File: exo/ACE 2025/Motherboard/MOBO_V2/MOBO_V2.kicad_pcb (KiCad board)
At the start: 4 copper layers, 100 x 100 mm, 70 parts, among them J301 USB_C_UART, J302 USB_C_DEBUG, J601 Conn_02x10_Counter_Clockwise, J602 Micro_SD_Card, J701 RJ45, J702 RJ45, J703 RJ45, Q201 AO3401A, U201 AP7361C-33E, U202 TPS562242DRLR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

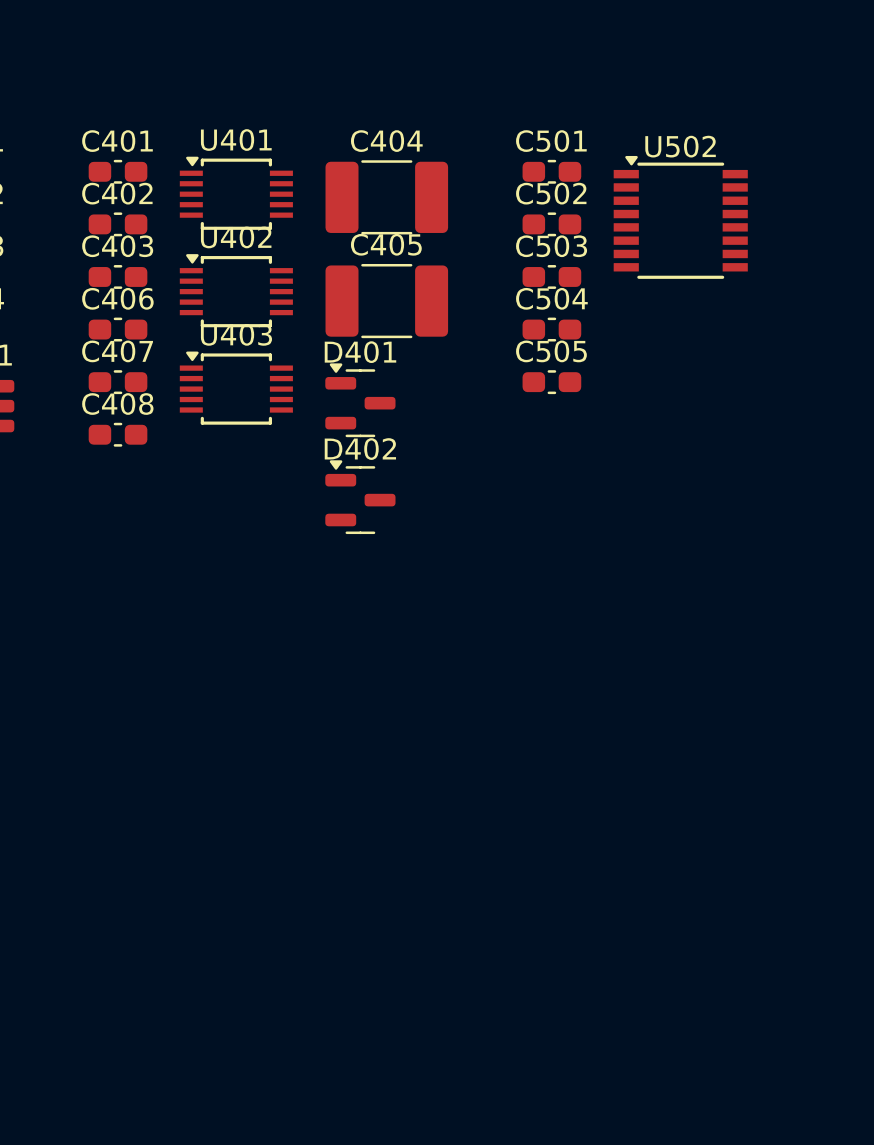
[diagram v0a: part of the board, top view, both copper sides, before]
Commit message: ajout infromation et d'épaisseur des traces selon le netclass et de joli couleur hehe
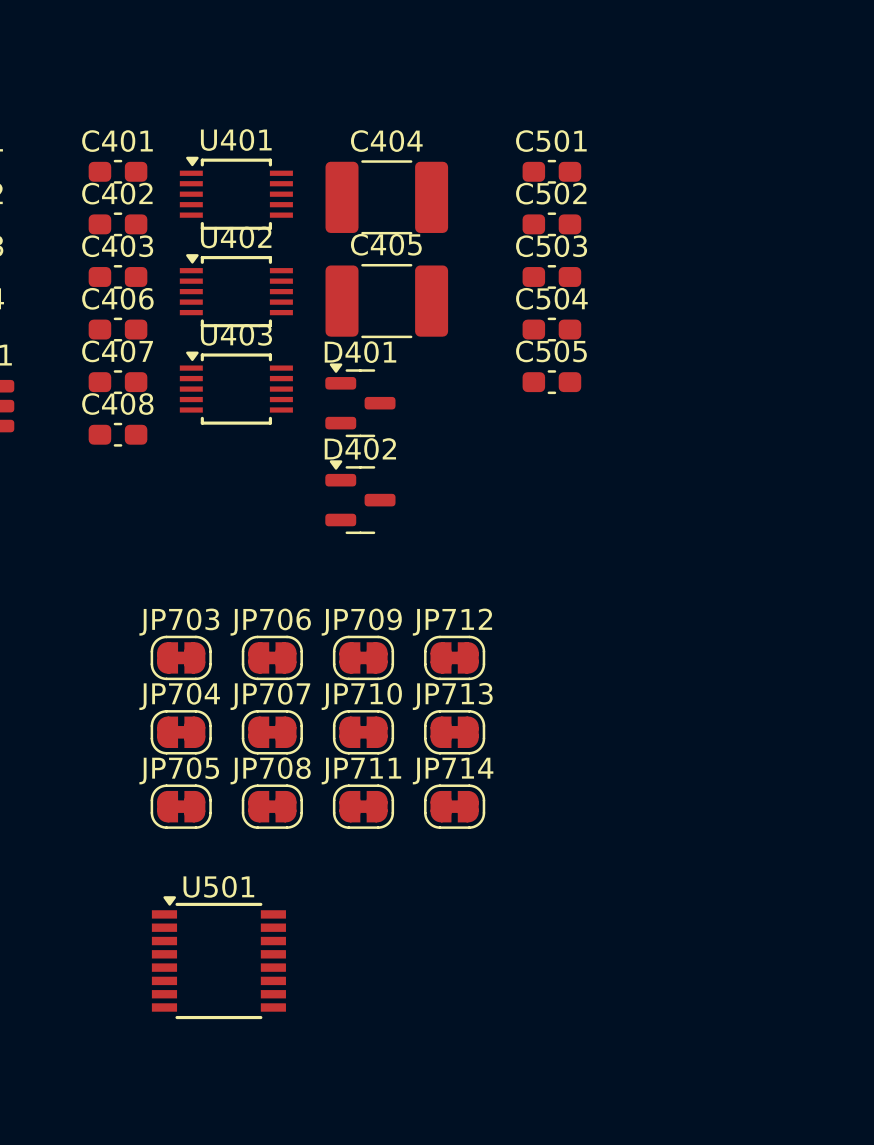
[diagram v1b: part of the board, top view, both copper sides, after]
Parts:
- removed U502: MAX3221, Package_SO:SSOP-16_3.9x4.9mm_P0.635mm
- added JP703: SolderJumper_2_Bridged, Jumper:SolderJumper-2_P1.3mm_Bridged_RoundedPad1.0x1.5mm, F.Cu at (42.5, 106.9)
- added JP704: SolderJumper_2_Bridged, Jumper:SolderJumper-2_P1.3mm_Bridged_RoundedPad1.0x1.5mm, F.Cu at (42.5, 110.4)
- added JP705: SolderJumper_2_Bridged, Jumper:SolderJumper-2_P1.3mm_Bridged_RoundedPad1.0x1.5mm, F.Cu at (42.5, 114.0)
- added JP706: SolderJumper_2_Bridged, Jumper:SolderJumper-2_P1.3mm_Bridged_RoundedPad1.0x1.5mm, F.Cu at (46.9, 106.9)
- added JP707: SolderJumper_2_Bridged, Jumper:SolderJumper-2_P1.3mm_Bridged_RoundedPad1.0x1.5mm, F.Cu at (46.9, 110.4)
- added JP708: SolderJumper_2_Bridged, Jumper:SolderJumper-2_P1.3mm_Bridged_RoundedPad1.0x1.5mm, F.Cu at (46.9, 114.0)
- added JP709: SolderJumper_2_Bridged, Jumper:SolderJumper-2_P1.3mm_Bridged_RoundedPad1.0x1.5mm, F.Cu at (51.2, 106.9)
- added JP710: SolderJumper_2_Bridged, Jumper:SolderJumper-2_P1.3mm_Bridged_RoundedPad1.0x1.5mm, F.Cu at (51.2, 110.4)
- added JP711: SolderJumper_2_Bridged, Jumper:SolderJumper-2_P1.3mm_Bridged_RoundedPad1.0x1.5mm, F.Cu at (51.2, 114.0)
- added JP712: SolderJumper_2_Bridged, Jumper:SolderJumper-2_P1.3mm_Bridged_RoundedPad1.0x1.5mm, F.Cu at (55.6, 106.9)
- added JP713: SolderJumper_2_Bridged, Jumper:SolderJumper-2_P1.3mm_Bridged_RoundedPad1.0x1.5mm, F.Cu at (55.6, 110.4)
- added JP714: SolderJumper_2_Bridged, Jumper:SolderJumper-2_P1.3mm_Bridged_RoundedPad1.0x1.5mm, F.Cu at (55.6, 114.0)
- added U501: MAX3221, Package_SO:SSOP-16_3.9x4.9mm_P0.635mm, F.Cu at (44.4, 121.3)
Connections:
- J701 pad 3: /Connecteurs/DOS.SCL1 -> /Connecteurs/DOS_SCL+
- J701 pad 4: /Connecteurs/DOS.SCL2 -> /Connecteurs/DOS_SCL-
- J701 pad 5: /Connecteurs/DOS.SDA1 -> /Connecteurs/DOS_SDA+
- J701 pad 6: /Connecteurs/DOS.SDA2 -> /Connecteurs/DOS_SDA-
- J702 pad 3: /Connecteurs/D.SCL1 -> /Connecteurs/D_SCL+
- J702 pad 4: /Connecteurs/D.SCL2 -> /Connecteurs/D_SCL-
- J702 pad 5: /Connecteurs/D.SDA1 -> /Connecteurs/D_SDA+
- J702 pad 6: /Connecteurs/D.SDA2 -> /Connecteurs/D_SDA-
- J703 pad 3: /Connecteurs/G.SCL1 -> /Connecteurs/G_SCL+
- J703 pad 4: /Connecteurs/G.SCL2 -> /Connecteurs/G_SCL-
- J703 pad 5: /Connecteurs/G.SDA1 -> /Connecteurs/G_SDA+
- J703 pad 6: /Connecteurs/G.SDA2 -> /Connecteurs/G_SDA-

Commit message: Commencement de la section I2C du PCB
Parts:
- J701 DOS: renamed from J701
- J702 DROITE: renamed from J702
- J703 GAUCHE: renamed from J703
- moved J703 GAUCHE 137.7 mm to (178.8, 124.6)
- moved J702 DROITE 126.9 mm to (148.8, 124.3)
- moved J701 DOS 115.4 mm to (117.6, 123.8)
- moved C403 95.2 mm to (132.8, 107.4)
- moved C408 92.8 mm to (130.3, 115.2)
- moved U403 88.2 mm to (131.7, 111.4), turned to 180 degrees
- moved D402 84.5 mm to (135.1, 89.9)
- moved D401 84.0 mm to (135.1, 96.4)
- moved JP704 81.2 mm to (123.4, 118.1), turned to 180 degrees
- moved JP703 78.5 mm to (120.8, 113.0), turned to 180 degrees
- moved C404 78.0 mm to (129.5, 96.3), turned to 90 degrees
- moved JP708 77.8 mm to (124.6, 115.6), turned to 180 degrees
- moved C405 77.2 mm to (129.5, 89.9), turned to 90 degrees
- moved JP707 75.0 mm to (121.9, 110.5), turned to 180 degrees
- moved JP714 17.3 mm to (72.6, 117.1)
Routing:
- net GND: track 0.00 -> 20.5 mm, vias 0 -> 2
- net Vcc_3V3: track 0.00 -> 18.7 mm
- net I2C_SDA_ESP32: track 0.00 -> 16.0 mm
- net I2C_SCL_ESP32: track 0.00 -> 12.9 mm
- net /Connecteurs/DOS.SDA2: track 0.00 -> 11.6 mm
- net /Connecteurs/DOS.SDA1: track 0.00 -> 11.4 mm, vias 0 -> 2
- net /Connecteurs/DOS_SCL-: track 0.00 -> 11.1 mm, vias 0 -> 1
- net /Connecteurs/DOS_SCL+: track 0.00 -> 10.8 mm
- net /Connecteurs/DOS.SCL1: track 0.00 -> 8.94 mm
- net /Connecteurs/DOS.SCL2: track 0.00 -> 8.89 mm
- net /Connecteurs/DOS_SDA-: track 0.00 -> 5.79 mm, vias 0 -> 1
- net /Connecteurs/DOS_SDA+: track 0.00 -> 5.77 mm
- net Vcc_5V: track 0.00 -> 2.86 mm

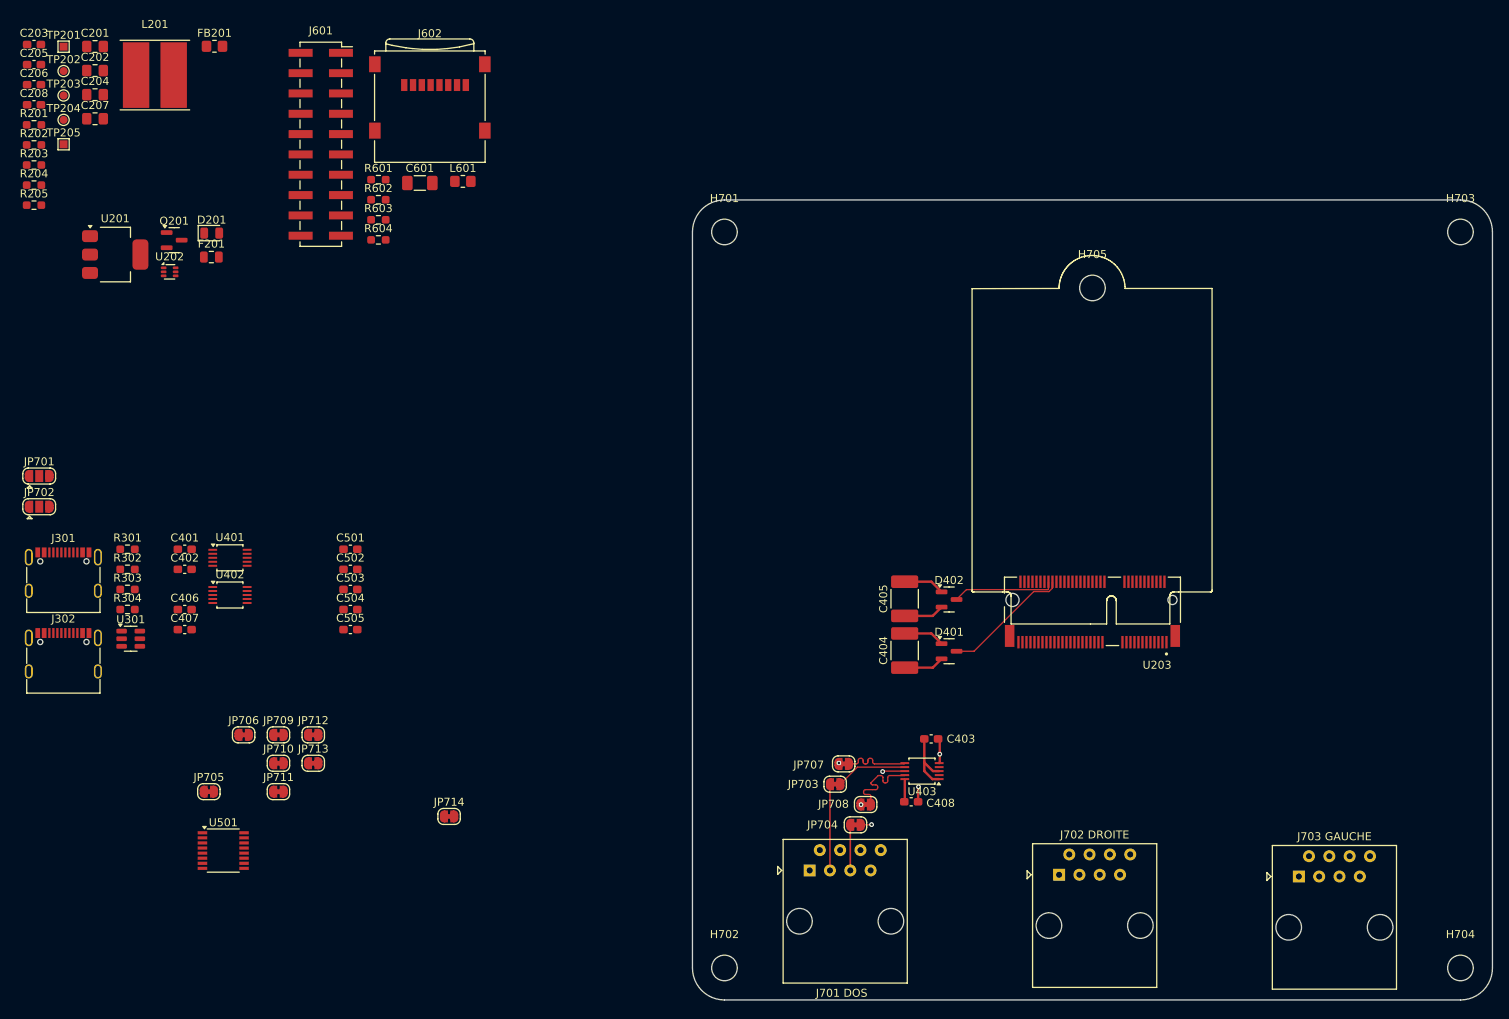
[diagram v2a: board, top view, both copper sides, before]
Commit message: Refaire le circuit I2C différentiel
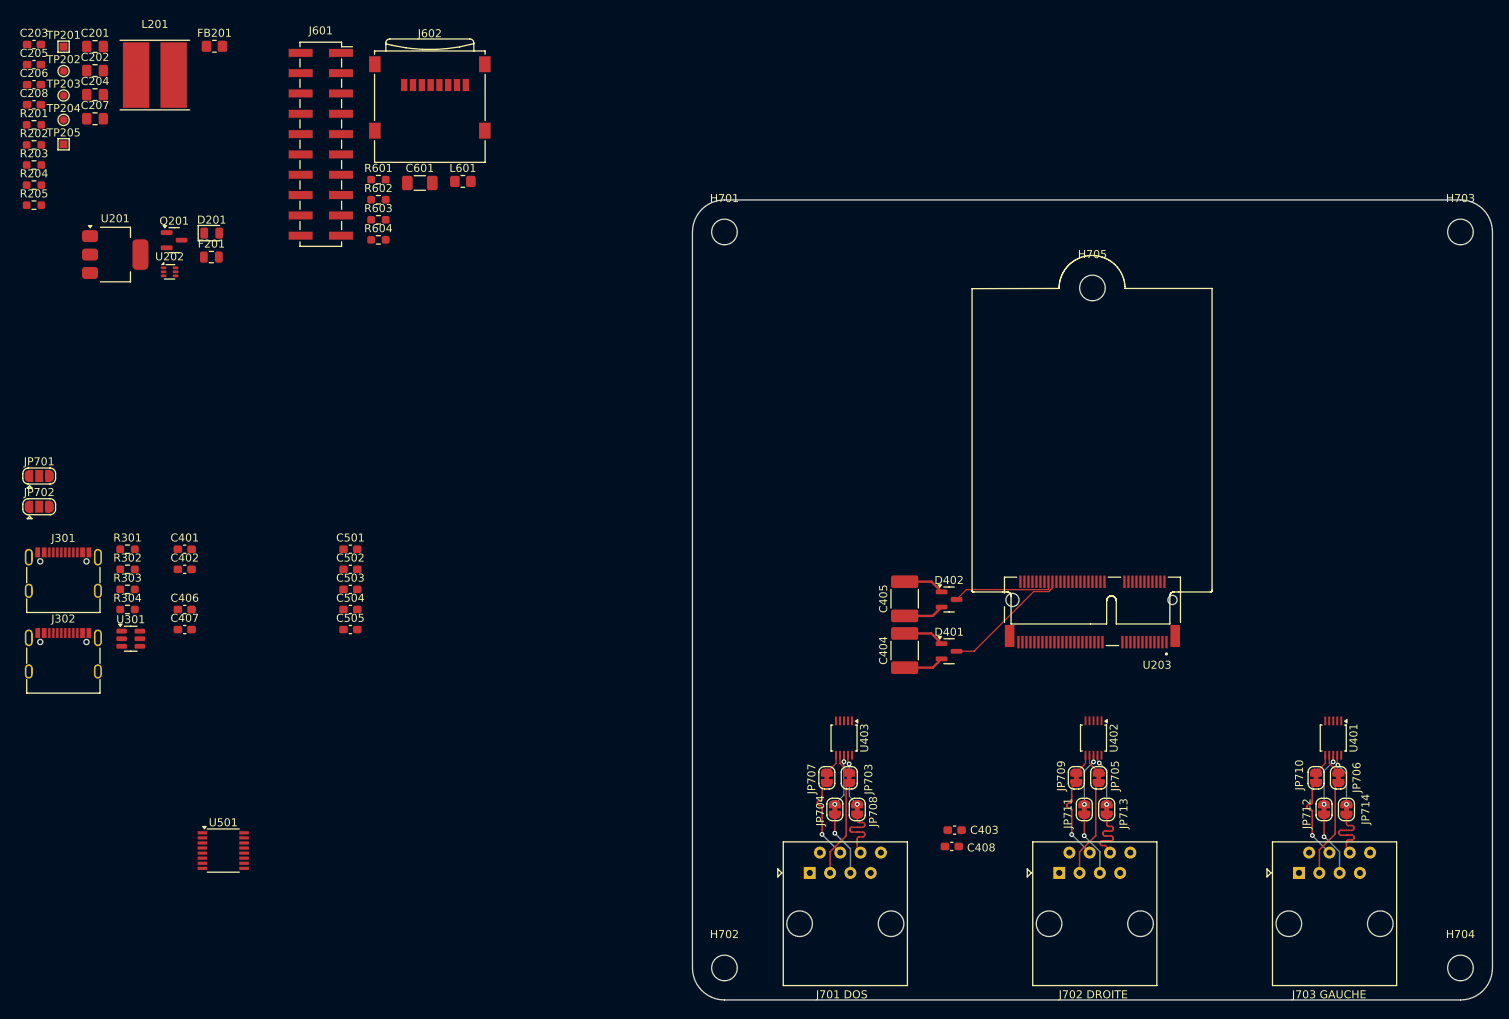
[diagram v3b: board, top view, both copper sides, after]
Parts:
- moved U401 139.7 mm to (183.1, 107.3), turned to -90 degrees
- moved JP706 137.0 mm to (183.8, 112.2), turned to -90 degrees
- moved JP710 129.7 mm to (180.9, 112.2), turned to -90 degrees
- moved JP712 126.7 mm to (181.9, 116.2), turned to -90 degrees
- moved JP714 112.2 mm to (184.8, 116.2), turned to -90 degrees
- moved JP705 111.2 mm to (153.8, 112.2), turned to -90 degrees
- moved U402 109.4 mm to (153.1, 107.3), turned to -90 degrees
- moved JP711 100.8 mm to (152.0, 116.2), turned to -90 degrees
- moved JP709 99.9 mm to (151.0, 112.2), turned to -90 degrees
- moved JP713 99.3 mm to (154.8, 116.2), turned to -90 degrees
- moved C403 11.8 mm to (135.8, 118.8)
- moved U403 10.6 mm to (121.9, 107.3), turned to -90 degrees
- moved C408 7.55 mm to (135.4, 120.8)
- moved JP704 3.22 mm to (120.8, 116.2), turned to -90 degrees
- moved JP707 2.73 mm to (119.8, 112.2), turned to -90 degrees
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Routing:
- net /Connecteurs/D_SCL+: track 0.00 -> 12.2 mm
- net /Connecteurs/G_SCL+: track 0.00 -> 12.2 mm
- net /Connecteurs/G_SCL-: track 0.00 -> 10.6 mm, vias 0 -> 1
- net /Connecteurs/D_SCL-: track 0.00 -> 10.6 mm, vias 0 -> 1
- net GND: track 20.5 -> 10.3 mm, vias 2 -> 0
- net /Connecteurs/G_SDA-: track 0.00 -> 9.65 mm
- net /Connecteurs/D_SDA-: track 0.00 -> 9.59 mm
- net Vcc_3V3: track 18.7 -> 10.1 mm
- net /Connecteurs/G_SDA+: track 0.00 -> 8.13 mm, vias 0 -> 1
- net /Connecteurs/D_SDA+: track 0.00 -> 8.09 mm, vias 0 -> 1
- net /Connecteurs/G.SDA2: track 0.00 -> 6.61 mm, vias 0 -> 2
- net /Connecteurs/G.SDA1: track 0.00 -> 6.61 mm, vias 0 -> 2
- net /Connecteurs/D.SDA2: track 0.00 -> 6.61 mm, vias 0 -> 2
- net /Connecteurs/D.SDA1: track 0.00 -> 6.61 mm, vias 0 -> 2
- net /Connecteurs/DOS.SCL1: track 8.94 -> 2.65 mm
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
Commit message: Commencement du circuit 3.3V
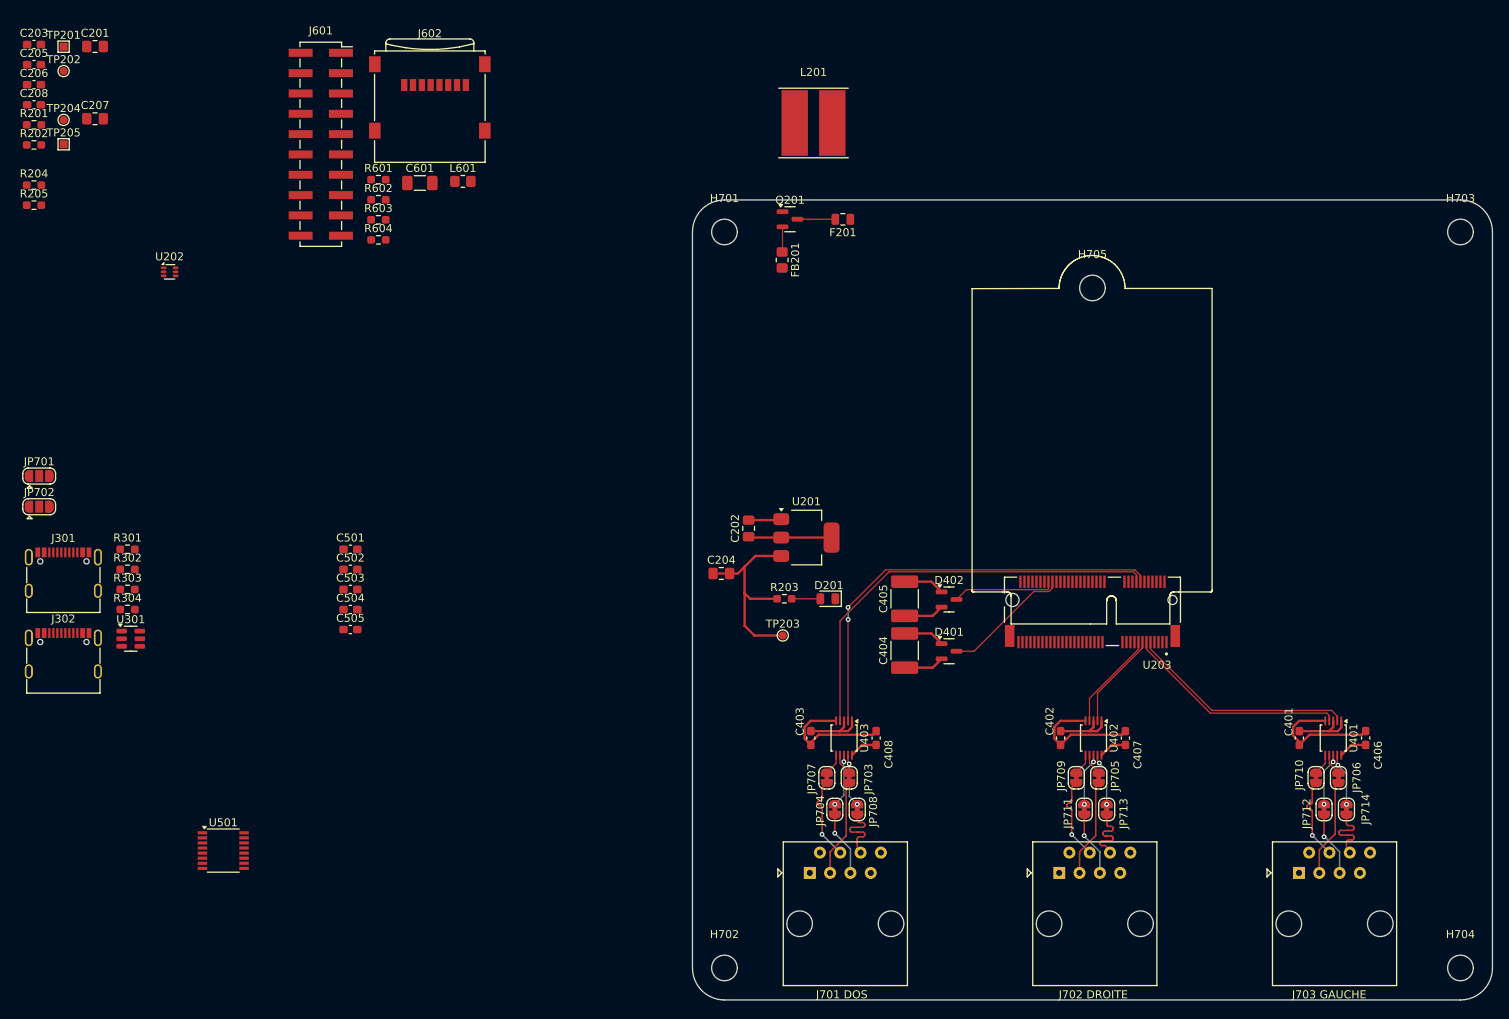
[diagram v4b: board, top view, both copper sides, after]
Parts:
- moved C406 148.5 mm to (187.2, 107.3), turned to 90 degrees
- moved C401 141.3 mm to (178.9, 107.3), turned to -90 degrees
- moved C407 118.4 mm to (157.1, 107.3), turned to 90 degrees
- moved TP203 112.4 mm to (114.3, 94.4)
- moved C402 111.5 mm to (149.0, 107.3), turned to -90 degrees
- moved R203 108.3 mm to (114.5, 89.8)
- moved C202 99.7 mm to (110.0, 81.1), turned to 90 degrees
- moved C204 98.5 mm to (106.6, 86.7)
- moved U201 93.4 mm to (117.2, 82.2)
- moved D201 89.6 mm to (119.9, 89.8), turned to 180 degrees
- moved L201 82.5 mm to (118.1, 30.4)
- moved F201 79.1 mm to (121.8, 42.4), turned to 180 degrees
- moved Q201 77.0 mm to (115.2, 42.4)
- moved FB201 75.8 mm to (114.2, 47.5), turned to -90 degrees
- moved C403 21.3 mm to (117.8, 107.3), turned to -90 degrees
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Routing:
- net GND: track 10.3 -> 68.1 mm
- net /I2C_w_Protection/I2C_SDA_2_TCA: track 0.00 -> 53.8 mm, vias 0 -> 2
- net /I2C_w_Protection/I2C_SCL_2_TCA: track 0.00 -> 53.1 mm
- net Vcc_3V3: track 10.1 -> 58.9 mm
- net /I2C_w_Protection/I2C_SDA_0_TCA: track 0.00 -> 28.3 mm
- net /I2C_w_Protection/I2C_SCL_0_TCA: track 0.00 -> 27.8 mm
- net Vcc_5V: track 0.00 -> 14.8 mm
- net /I2C_w_Protection/I2C_SCL_1_TCA: track 0.00 -> 12.4 mm
- net /I2C_w_Protection/I2C_SDA_1_TCA: track 0.00 -> 12.2 mm
- net Net-(Q201-D): track 0.00 -> 4.73 mm
- net Net-(D201-A): track 0.00 -> 3.58 mm
- net Net-(Q201-S): track 0.00 -> 3.16 mm
